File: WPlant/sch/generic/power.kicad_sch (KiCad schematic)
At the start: 41 parts, among them J2 Battery, J3 Balance, J4 DE9_Receptacle, J5 220V, U2 AP64352SP-13, U3 AP64352SP-13, U4 AP64352SP-13, U6 AP2204R-5.0

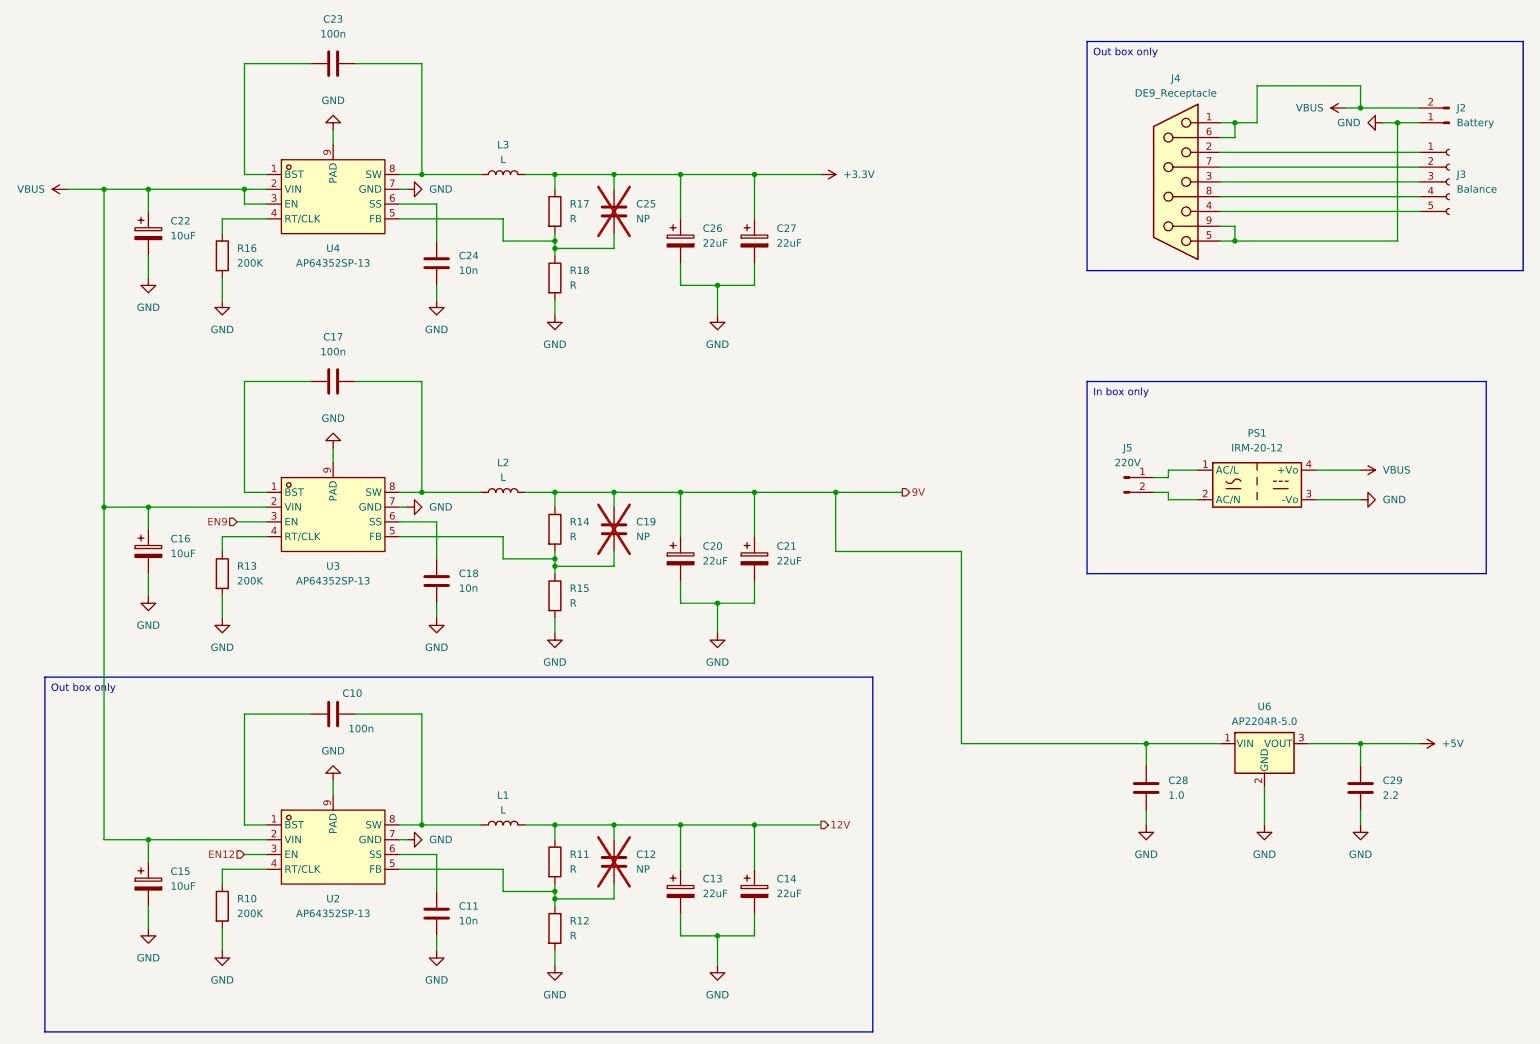
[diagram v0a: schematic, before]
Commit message: Generic schematic almost done
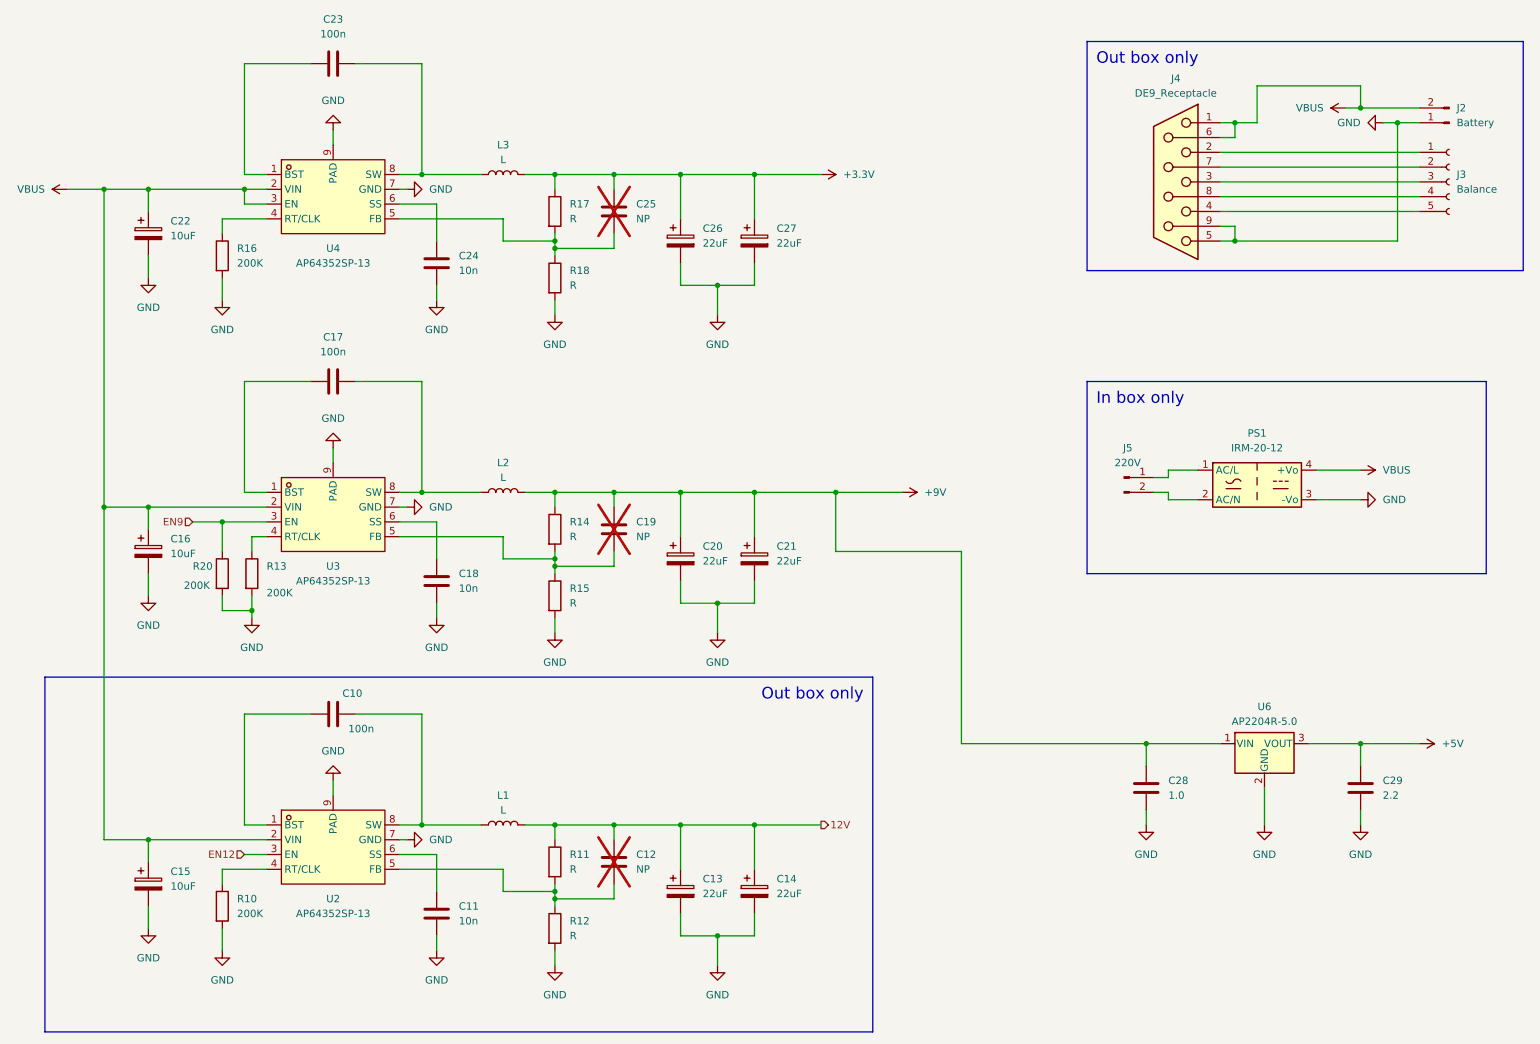
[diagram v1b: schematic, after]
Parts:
- added R20: 200K, symbol Device:R
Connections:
- net EN9: now also R20.1
- net GND: now also R20.2
- net 9V renamed +9V
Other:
- company: (none) -> RoboWay
- title: (none) -> Power module
- moved on the sheet: R13
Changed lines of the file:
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@@
 	(generator_version "8.0")
 	(paper "A4")
+	(title_block
+		(title "Power module")
+		(company "RoboWay")
+	)
 	(junction
 		(at 129.54 96.52)
@@
 	)
 	(junction
+		(at 50.8 101.6)
+		(diameter 0)
+		(color 0 0 0 0)
+	)
+	(junction
 		(at 107.95 107.95)
 		(diameter 0)
@@
 	)
 	(junction
+		(at 55.88 116.84)
+		(diameter 0)
+		(color 0 0 0 0)
+	)
+	(junction
 		(at 142.24 153.67)
 		(diameter 0)
@@
 	(wire
 		(pts
+			(xy 50.8 114.3) (xy 50.8 116.84)
+		)
+		(stroke
+			(width 0)
+			(type default)
+		)
+	)
+	(wire
+		(pts
 			(xy 222.25 48.26) (xy 256.54 48.26)
 		)
@@
 	(wire
 		(pts
+			(xy 50.8 101.6) (xy 58.42 101.6)
+		)
+		(stroke
+			(width 0)
+			(type default)
+		)
+	)
+	(wire
+		(pts
 			(xy 135.89 115.57) (xy 135.89 120.65)
 		)
@@
 	(wire
 		(pts
-			(xy 50.8 104.14) (xy 58.42 104.14)
+			(xy 55.88 104.14) (xy 58.42 104.14)
 		)
 		(stroke
@@
 	(wire
 		(pts
+			(xy 55.88 114.3) (xy 55.88 116.84)
+		)
+		(stroke
+			(width 0)
+			(type default)
+		)
+	)
+	(wire
+		(pts
 			(xy 99.06 53.34) (xy 107.95 53.34)
 		)
@@
 	(wire
 		(pts
-			(xy 50.8 114.3) (xy 50.8 118.11)
+			(xy 99.06 161.29) (xy 99.06 165.1)
 		)
 		(stroke
@@
 	(wire
 		(pts
-			(xy 99.06 161.29) (xy 99.06 165.1)
+			(xy 224.79 53.34) (xy 252.73 53.34)
 		)
 		(stroke
@@
 	(wire
 		(pts
-			(xy 224.79 53.34) (xy 252.73 53.34)
+			(xy 50.8 116.84) (xy 55.88 116.84)
 		)
 		(stroke
@@
 	(wire
 		(pts
+			(xy 50.8 101.6) (xy 50.8 106.68)
+		)
+		(stroke
+			(width 0)
+			(type default)
+		)
+	)
+	(wire
+		(pts
 			(xy 222.25 40.64) (xy 256.54 40.64)
 		)
@@
 	(wire
 		(pts
-			(xy 50.8 106.68) (xy 50.8 104.14)
+			(xy 55.88 106.68) (xy 55.88 104.14)
 		)
 		(stroke
@@
 	(wire
 		(pts
+			(xy 55.88 116.84) (xy 55.88 118.11)
+		)
+		(stroke
+			(width 0)
+			(type default)
+		)
+	)
+	(wire
+		(pts
 			(xy 222.25 38.1) (xy 256.54 38.1)
 		)
@@
 	(wire
 		(pts
-			(xy 53.34 101.6) (xy 58.42 101.6)
+			(xy 45.72 101.6) (xy 50.8 101.6)
 		)
 		(stroke
@@
 		)
 		(fill
-			(type none)
+			(type color)
+			(color 197 255 210 1)
 		)
 		(effects
 			(font
-				(size 1.27 1.27)
+				(size 2 2)
 			)
 			(justify left top)
@@
 		)
 		(fill
-			(type none)
+			(type color)
+			(color 190 204 255 1)
 		)
 		(effects
 			(font
-				(size 1.27 1.27)
+				(size 2 2)
 			)
 			(justify left top)
@@
 		)
 		(fill
-			(type none)
+			(type color)
+			(color 197 255 210 1)
 		)
 		(effects
 			(font
-				(size 1.27 1.27)
+				(size 2 2)
 			)
-			(justify left top)
+			(justify right top)
 		)
 	)
 	(hierarchical_label "EN9"
 		(shape input)
-		(at 53.34 101.6 180)
+		(at 45.72 101.6 180)
 		(fields_autoplaced yes)
 		(effects
@@
 		)
 	)
-	(hierarchical_label "9V"
-		(shape output)
-		(at 167.64 96.52 0)
-		(fields_autoplaced yes)
-		(effects
-			(font
-				(size 1.27 1.27)
-			)
-			(justify left)
-		)
-	)
 	(hierarchical_label "12V"
 		(shape output)
@@
 	(symbol
 		(lib_id "power:GND")
-		(at 50.8 118.11 0)
+		(at 55.88 118.11 0)
 		(unit 1)
 		(exclude_from_sim no)
@@
 		(fields_autoplaced yes)
 		(property "Reference" "#PWR026"
-			(at 50.8 124.46 0)
+			(at 55.88 124.46 0)
 			(effects
 				(font
@@
 		)
 		(property "Value" "GND"
-			(at 50.8 123.19 0)
+			(at 55.88 123.19 0)
 			(effects
 				(font
@@
 		)
 		(property "Footprint" ""
-			(at 50.8 118.11 0)
+			(at 55.88 118.11 0)
 			(effects
 				(font
@@
 		)
 		(property "Datasheet" ""
-			(at 50.8 118.11 0)
+			(at 55.88 118.11 0)
 			(effects
 				(font
@@
 		)
 		(property "Description" "Power symbol creates a global label with name \"GND\" , ground"
-			(at 50.8 118.11 0)
+			(at 55.88 118.11 0)
 			(effects
 				(font
@@
 	(symbol
 		(lib_id "Device:R")
-		(at 50.8 110.49 0)
+		(at 55.88 110.49 0)
 		(unit 1)
 		(exclude_from_sim no)
@@
 		(on_board yes)
 		(dnp no)
-		(fields_autoplaced yes)
 		(property "Reference" "R13"
-			(at 53.34 109.2199 0)
+			(at 58.42 109.2199 0)
 			(effects
 				(font
@@
 		)
 		(property "Value" "200K"
-			(at 53.34 111.7599 0)
+			(at 58.42 113.792 0)
 			(effects
 				(font
@@
 		)
 		(property "Footprint" ""
-			(at 49.022 110.49 90)
+			(at 54.102 110.49 90)
 			(effects
 				(font
@@
 		)
 		(property "Datasheet" "~"
-			(at 50.8 110.49 0)
+			(at 55.88 110.49 0)
 			(effects
 				(font
@@
 		)
 		(property "Description" "Resistor"
-			(at 50.8 110.49 0)
+			(at 55.88 110.49 0)
 			(effects
 				(font
@@
 	(symbol
 		(lib_id "Device:R")
+		(at 50.8 110.49 0)
+		(unit 1)
+		(exclude_from_sim no)
+		(in_bom yes)
+		(on_board yes)
+		(dnp no)
+		(property "Reference" "R20"
+			(at 45.72 109.22 0)
+			(effects
+				(font
+					(size 1.27 1.27)
+				)
+				(justify left)
+			)
+		)
+		(property "Value" "200K"
+			(at 44.196 112.522 0)
+			(effects
+				(font
+					(size 1.27 1.27)
+				)
+				(justify left)
+			)
+		)
+		(property "Footprint" ""
+			(at 49.022 110.49 90)
+			(effects
+				(font
+					(size 1.27 1.27)
+				)
+				(hide yes)
+			)
+		)
+		(property "Datasheet" "~"
+			(at 50.8 110.49 0)
+			(effects
+				(font
+					(size 1.27 1.27)
+				)
+				(hide yes)
+			)
+		)
+		(property "Description" "Resistor"
+			(at 50.8 110.49 0)
+			(effects
+				(font
+					(size 1.27 1.27)
+				)
+				(hide yes)
+			)
+		)
+		(pin "1"
+		)
+		(pin "2"
+		)
+		(instances
+			(project "generic"
+				(path "/71bd3f7f-463d-4a2c-bec7-ca56c2fe6cec/e5010fd4-921a-4703-b472-3554db39dd22"
+					(reference "R20")
+					(unit 1)
+				)
+			)
+		)
+	)
+	(symbol
+		(lib_id "Device:R")
 		(at 107.95 171.45 0)
 		(unit 1)
@@
 					(unit 1)
 				)
+			)
+		)
+	)
+	(symbol
+		(lib_id "power:+9V")
+		(at 167.64 96.52 270)
+		(unit 1)
+		(exclude_from_sim no)
+		(in_bom yes)
+		(on_board yes)
+		(dnp no)
+		(fields_autoplaced yes)
+		(property "Reference" "#PWR063"
+			(at 163.83 96.52 0)
+			(effects
+				(font
+					(size 1.27 1.27)
+				)
+				(hide yes)
+			)
+		)
+		(property "Value" "+9V"
+			(at 171.45 96.5199 90)
+			(effects
+				(font
+					(size 1.27 1.27)
+				)
+				(justify left)
+			)
+		)
+		(property "Footprint" ""
+			(at 167.64 96.52 0)
+			(effects
+				(font
+					(size 1.27 1.27)
+				)
+				(hide yes)
+			)
+		)
+		(property "Datasheet" ""
+			(at 167.64 96.52 0)
+			(effects
+				(font
+					(size 1.27 1.27)
+				)
+				(hide yes)
+			)
+		)
+		(property "Description" "Power symbol creates a global label with name \"+9V\""
+			(at 167.64 96.52 0)
+			(effects
+				(font
+					(size 1.27 1.27)
+				)
+				(hide yes)
+			)
+		)
+		(pin "1"
+		)
+		(instances
+			(project ""
+				(path "/71bd3f7f-463d-4a2c-bec7-ca56c2fe6cec/e5010fd4-921a-4703-b472-3554db39dd22"
+					(reference "#PWR063")
+					(unit 1)
+				)

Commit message: Updated Generic WP schematic
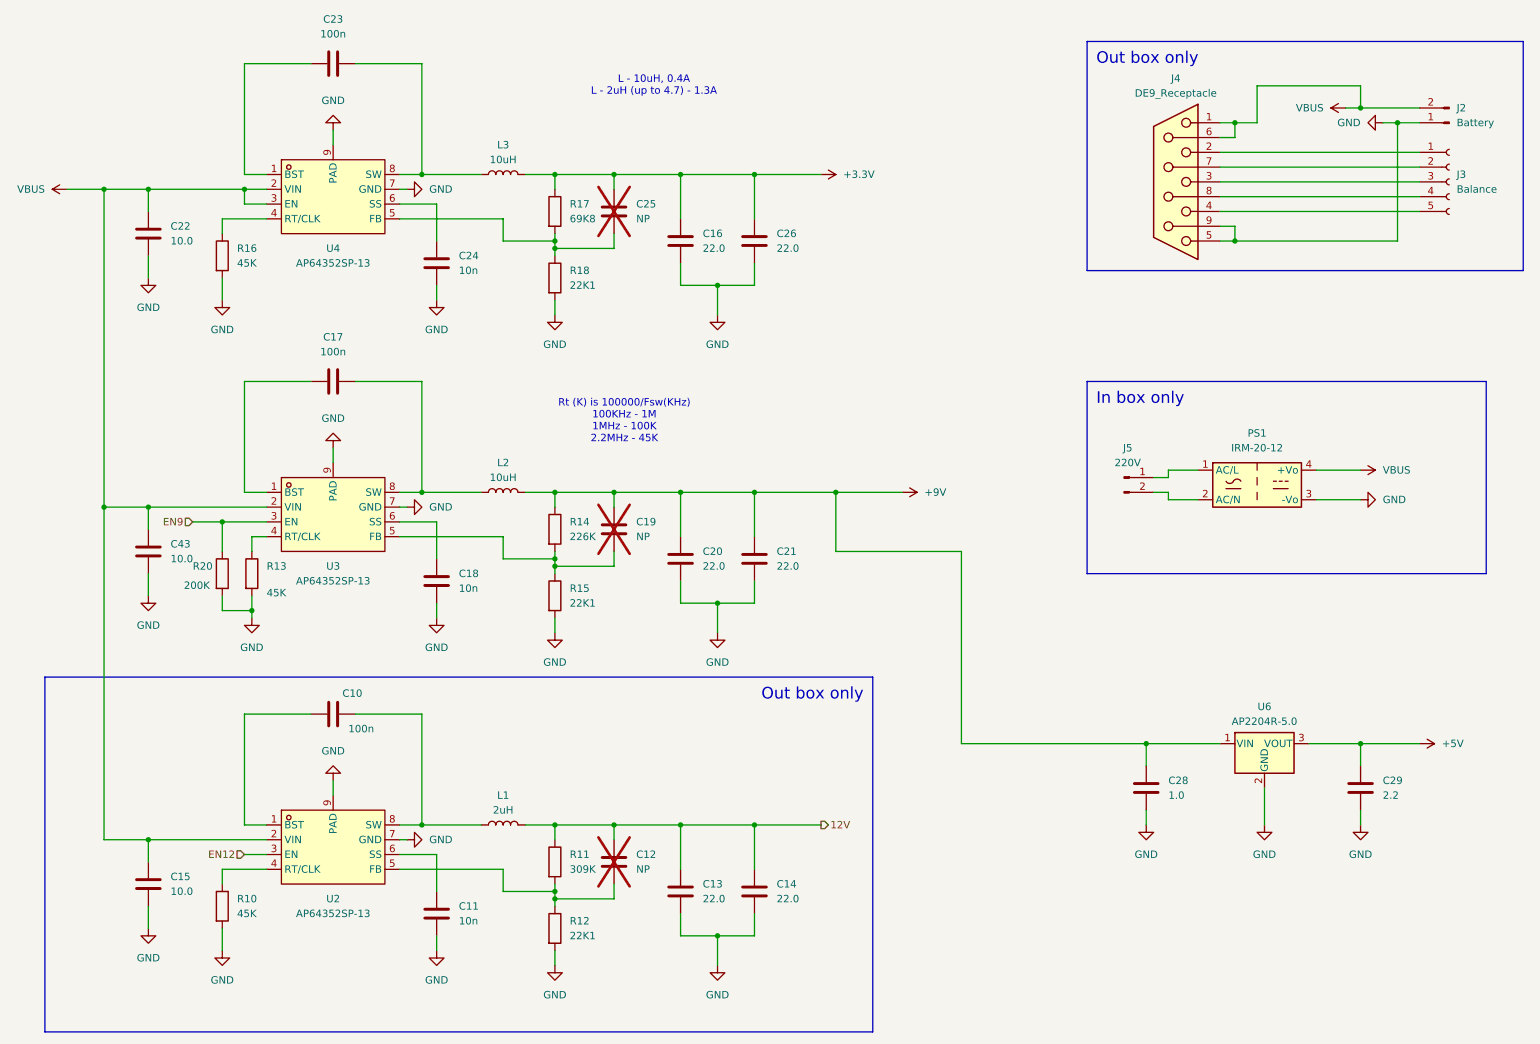
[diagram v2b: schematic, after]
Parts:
- removed C13, C14, C20, C21, C26, C27: 22uF, symbol Device:C_Polarized
- removed C15, C16, C22: 10uF, symbol Device:C_Polarized
- added C13, C14, C16, C20, C21, C26: 22.0, symbol Device:C
- added C15, C22, C43: 10.0, symbol Device:C
- L1: value L -> 2uH
- L2, L3: value L -> 10uH
- R10, R13, R16: value 200K -> 45K
- R11: value R -> 309K
- R12, R15, R18: value R -> 22K1
- R14: value R -> 226K
- R17: value R -> 69K8
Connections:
- net +3.3V: now also C16.2, C26.2
- net +9V: now also C20.2, C21.2
- net 12V: now also C13.2, C14.2
- net GND: now also C13.1, C14.1, C15.1, C16.1, C20.1, C21.1, C22.1, C26.1, C43.1
- net VBUS: now also C15.2, C22.2, C43.2
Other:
- note added: "L - 10uH, 0.4A L - 2uH (up to 4.7) - 1.3A"
- note added: "Rt (K) is 100000/Fsw(KHz) 100KHz - 1M 1MHz - 100K 2.2MHz - 45K"

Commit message: Update WP Extension and Generic
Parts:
- added C27, C44, C46, C47: 100, Capacitor_THT:CP_Radial_D5.0mm_P2.00mm, symbol Device:C_Polarized
- added C45: 1000, Capacitor_THT:CP_Radial_D8.0mm_P3.50mm, symbol Device:C_Polarized
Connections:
- net +3.3V: now also C27.1
- net +5V: now also C47.1
- net +9V: now also C44.1
- net 12V: now also C46.1
- net GND: now also C27.2, C44.2, C45.2, C46.2, C47.2
- net VBUS: now also C45.1
